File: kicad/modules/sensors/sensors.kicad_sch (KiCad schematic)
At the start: 48 parts, among them J1 Bus_PCI_Express_x1, J2 TYPE-C-31-M-04, J4 Conn_01x02, U2 RP2040, U4 W25Q128JVP, U5 BMP388, U8 BNO055, U9 MCP25625T-E/ML, X1 ABM8-272-T3, Y1 ABS07-32.768KHZ-T, Y2 X322516MLB4SI

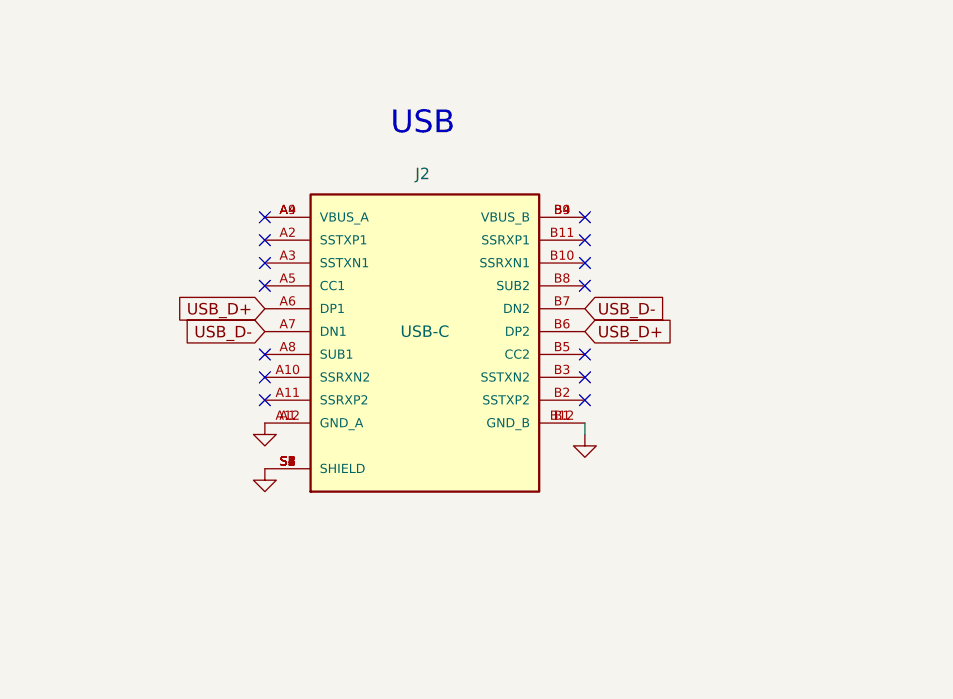
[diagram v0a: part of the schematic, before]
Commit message: change USB-C connector
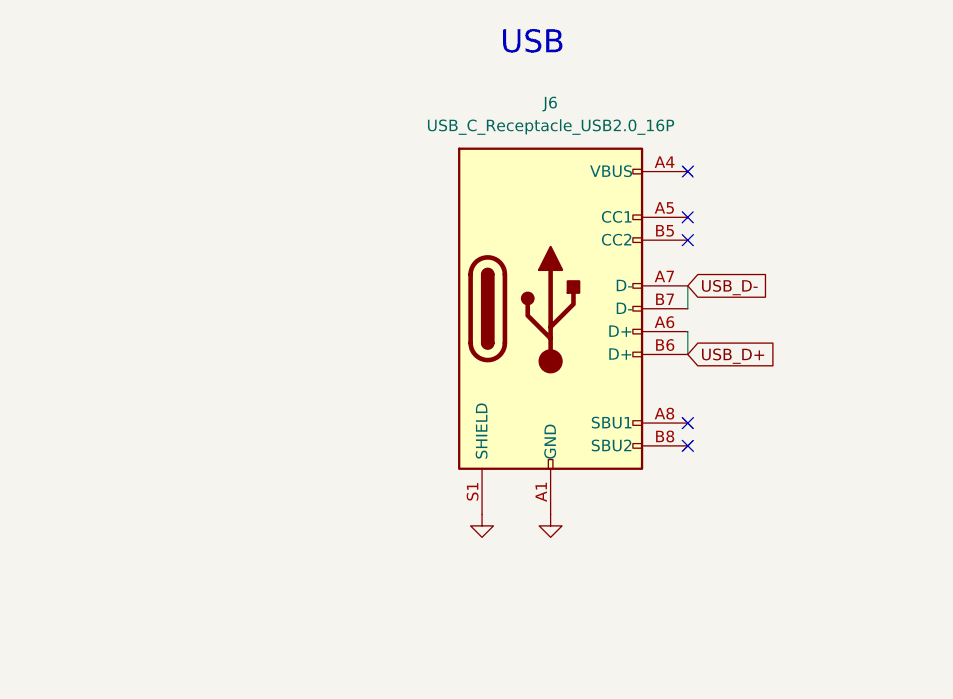
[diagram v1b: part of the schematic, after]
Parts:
- removed J2: TYPE-C-31-M-04, TYPE-C-31-M-04:HRO_TYPE-C-31-M-04, symbol TYPE-C-31-M-04:TYPE-C-31-M-04
- added J6: USB_C_Receptacle_USB2.0_16P, Connector_USB:USB_C_Receptacle_Palconn_UTC16-G, symbol Connector:USB_C_Receptacle_USB2.0_16P
- R203, R204: footprint Resistor_SMD:R_0603_1608Metric -> Resistor_SMD:R_0402_1005Metric; JLC Link https://jlcpcb.com/partdetail/25933-0603WAF270JT5E/C25190 -> https://jlcpcb.com/partdetail/25843-0402WGF270JTCE/C25100; LCSC Part # C25190 -> C25100; basic? extended prefered -> no; price C$0.0013 -> C$0.0007
- S1, S2: price C$0.0242 -> C$0.0242
- U5: price C$2.3423 -> C$2.3423
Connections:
- net GND: now also J6.A1 (GND), J6.A12 (GND), J6.B1 (GND), J6.B12 (GND), J6.S1 (SHIELD)
- net USB_D+: now also J6.A6 (D+), J6.B6 (D+)
- net USB_D-: now also J6.A7 (D-), J6.B7 (D-)
- new net: J6.A4 (VBUS), J6.A9 (VBUS), J6.B4 (VBUS), J6.B9 (VBUS)
- no-connect marks 20 -> 11

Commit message: route under rp2040
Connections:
- net USB_D2-: now reaches R204.2, U2.46 (USB_DM)
- net USB_D2+: now reaches R203.2, U2.47 (USB_DP)
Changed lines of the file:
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@@
+		)
+	)
+	(label "USB_D2+"
+		(at 262.89 151.13 0)
+		(fields_autoplaced yes)
+		(effects
+			(font
+				(size 1.27 1.27)
+			)
+			(justify left bottom)
 		)
 	)
@@
 		(fields_autoplaced yes)
 		(effects
+			(font
+				(size 1.27 1.27)
+			)
+			(justify left bottom)
+		)
+	)
+	(label "USB_D2-"
+		(at 262.89 153.67 0)
+		(fields_autoplaced yes)
+		(effects

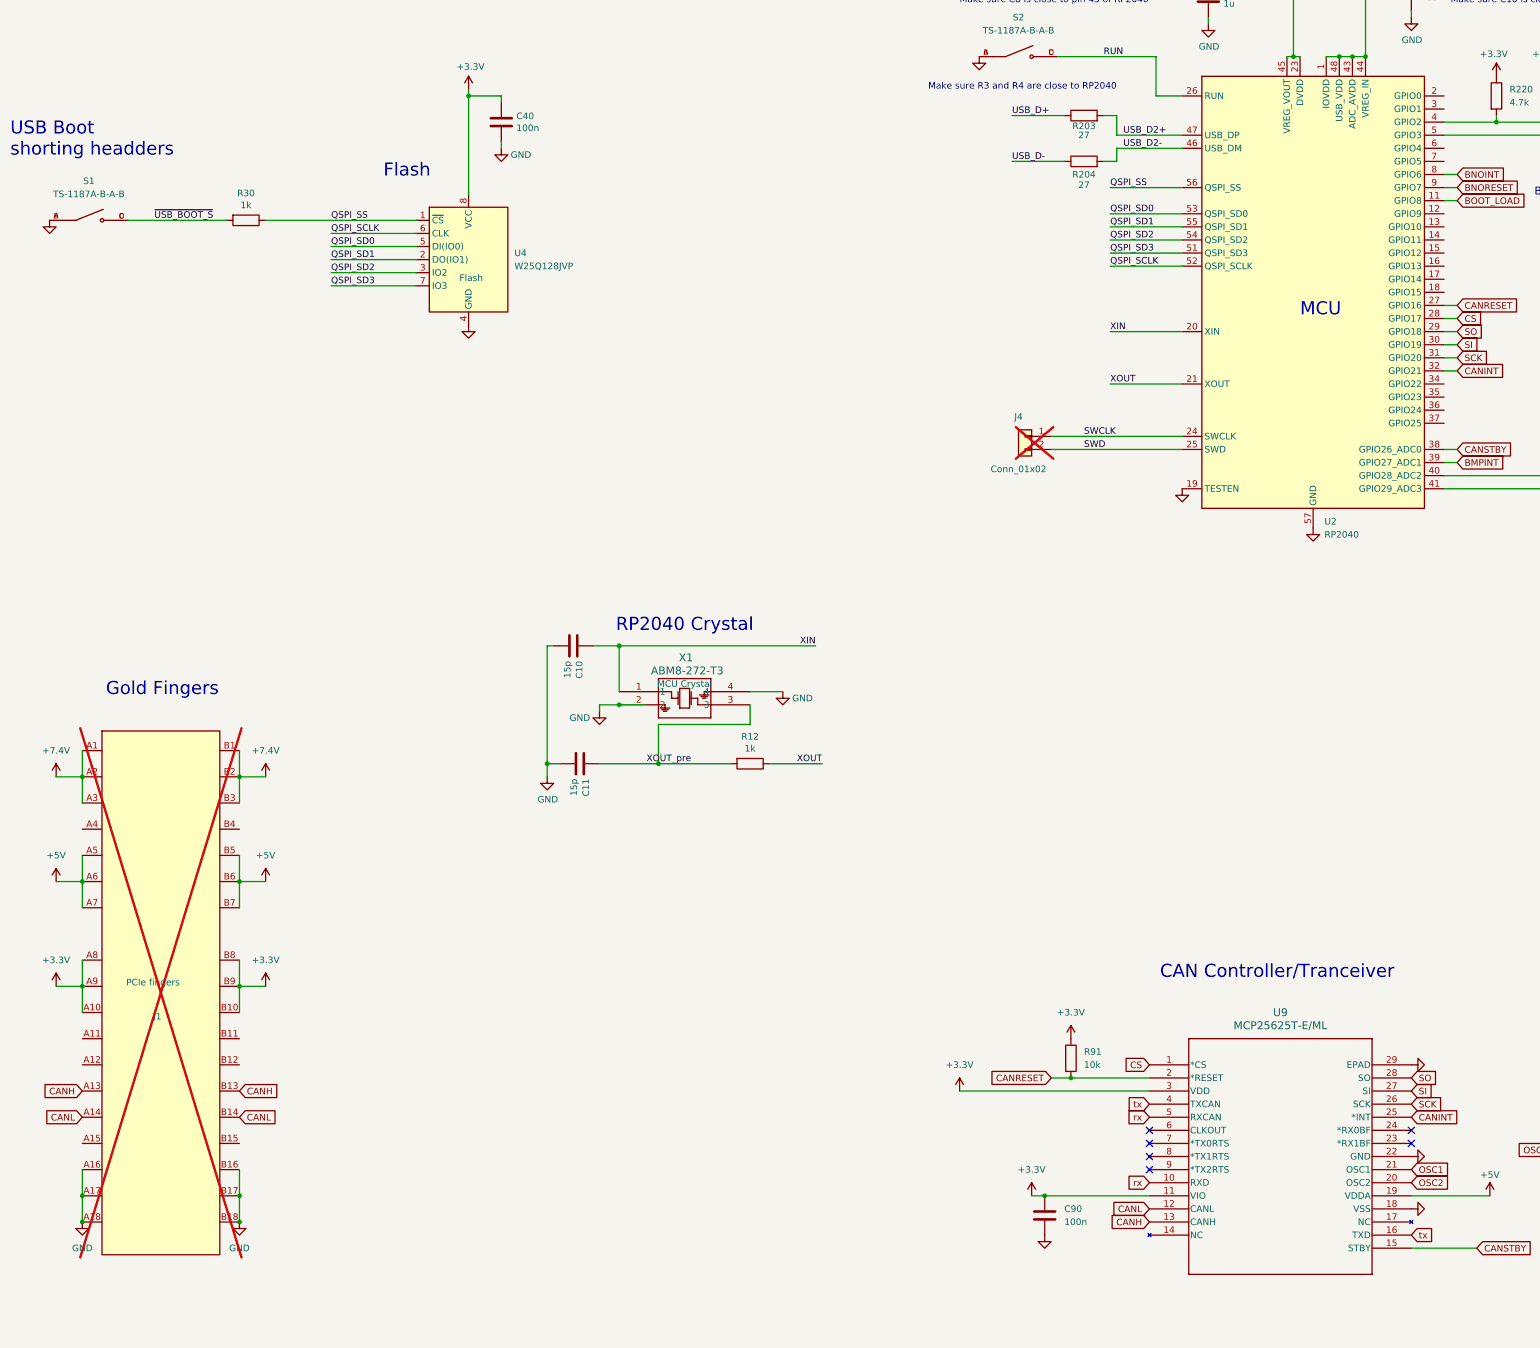
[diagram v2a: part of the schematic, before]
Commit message: complete all routing connections, and planes
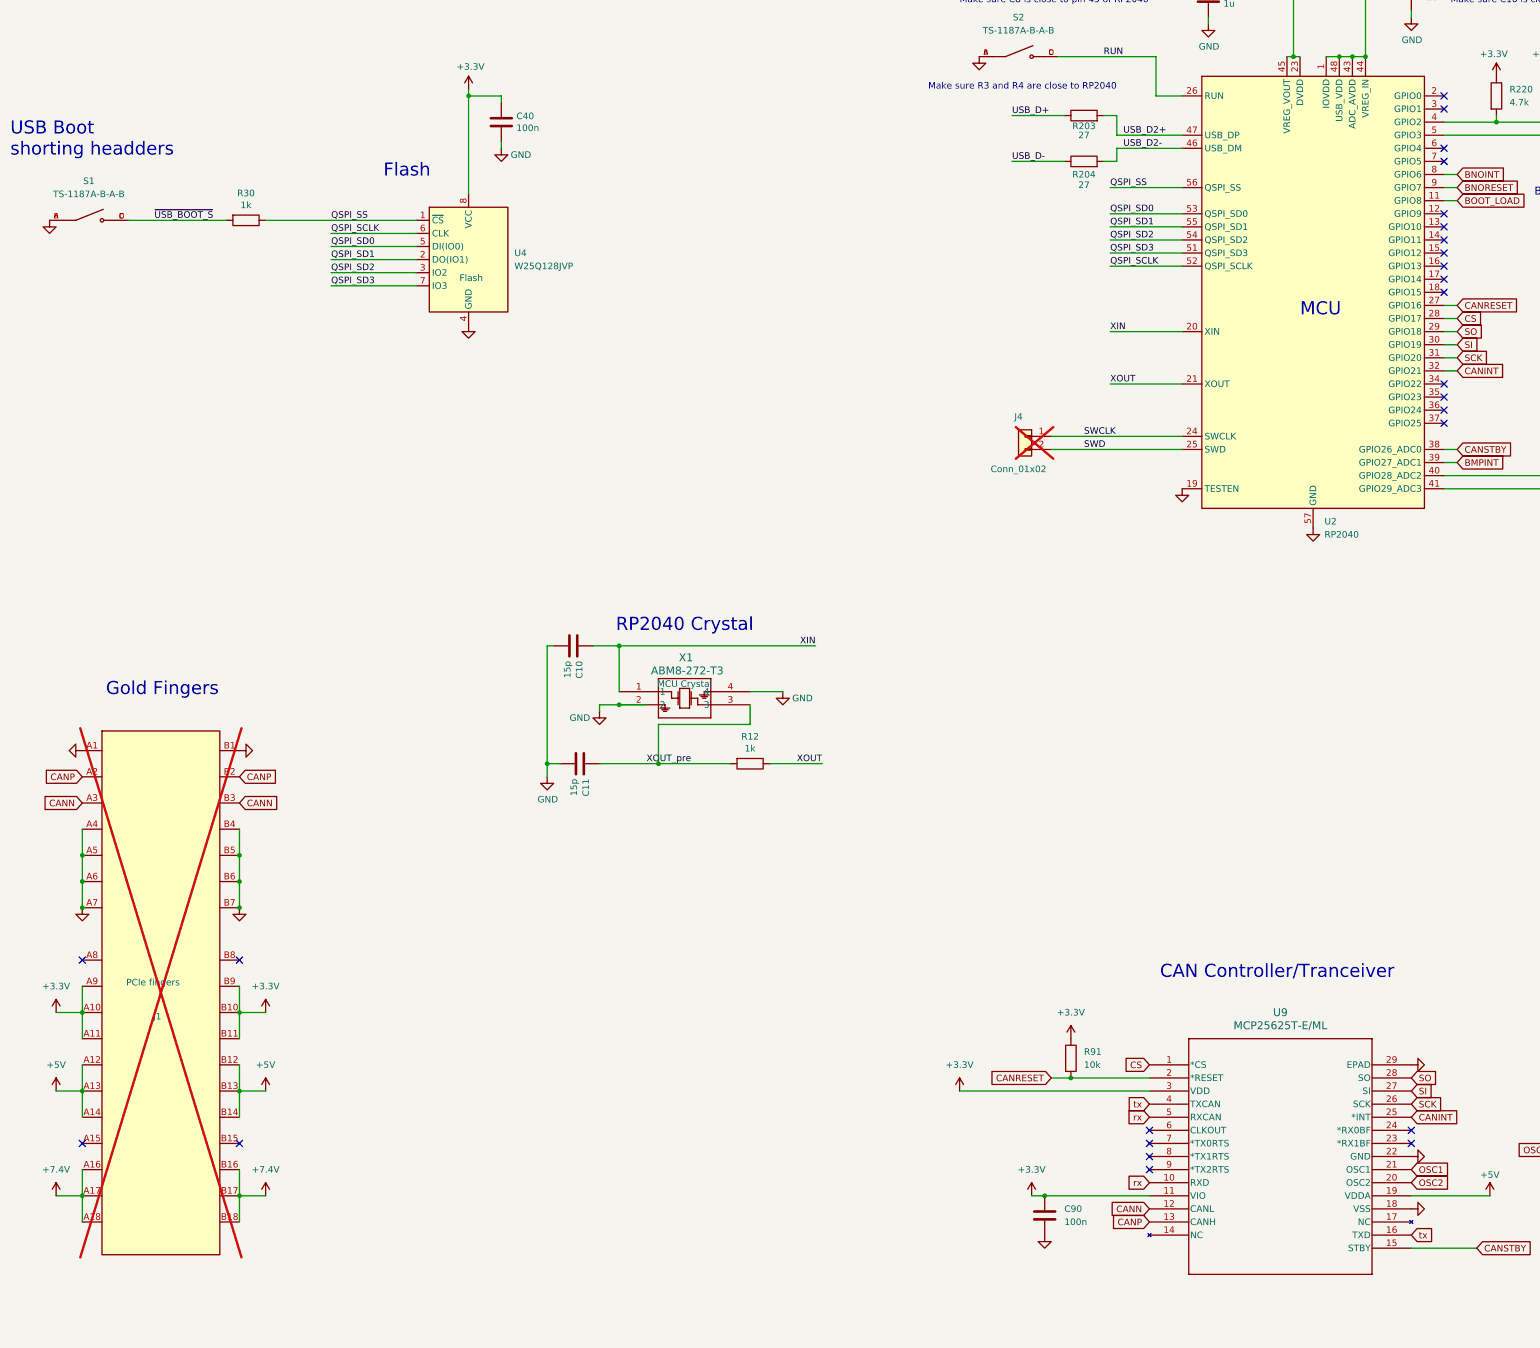
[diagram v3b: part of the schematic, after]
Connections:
- net +3.3V: now also J1.A11 (~{PERST}), J1.B11 (~{WAKE}); no longer J1.A8 (JTAG5), J1.B8 (+3.3V)
- net +5V: now also J1.A12 (GND), J1.A13 (REFCLK+), J1.A14 (REFCLK-), J1.B12 (RSVD), J1.B13 (GND), J1.B14 (PETp0); no longer J1.A5 (JTAG2), J1.A6 (JTAG3), J1.A7 (JTAG4), J1.B5 (SMCLK), J1.B6 (SMDAT), J1.B7 (GND)
- net +7.4V: now also J1.A16 (PERp0), J1.A17 (PERn0), J1.A18 (GND), J1.B16 (GND), J1.B17 (~{PRSNT2}), J1.B18 (GND); no longer J1.A1 (~{PRSNT1}), J1.A2 (+12V), J1.A3 (+12V), J1.B1 (+12V), J1.B2 (+12V), J1.B3 (+12V)
- net GND: now also J1.A1 (~{PRSNT1}), J1.A4 (GND), J1.A5 (JTAG2), J1.A6 (JTAG3), J1.A7 (JTAG4), J1.B1 (+12V), J1.B4 (GND), J1.B5 (SMCLK), J1.B6 (SMDAT), J1.B7 (GND); no longer J1.A16 (PERp0), J1.A17 (PERn0), J1.A18 (GND), J1.B16 (GND), J1.B17 (~{PRSNT2}), J1.B18 (GND)
- removed net CANH: J1.A13 (REFCLK+), J1.B13 (GND), U9.13 (CANH)
- removed net CANL: J1.A14 (REFCLK-), J1.B14 (PETp0), U9.12 (CANL)
- new net CANN: J1.A3 (+12V), J1.B3 (+12V), U9.12 (CANL)
- new net CANP: J1.A2 (+12V), J1.B2 (+12V), U9.13 (CANH)
- no-connect marks 11 -> 30

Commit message: refine routing
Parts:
- added C92, C93: 100n, Capacitor_SMD:C_0402_1005Metric, symbol Device:C
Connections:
- net +3.3V: now also C92.1
- net +5V: now also C93.1
- net GND: now also C92.2, C93.2
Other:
- note added: "Make sure C210 is close to pin 44 of RP2040"
- note removed: "Make sure C10 is close to pin 44 of RP2040"

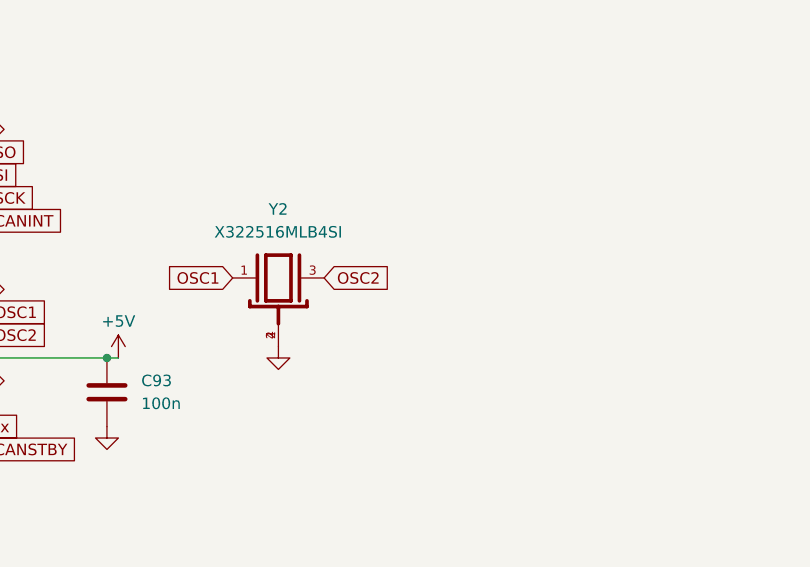
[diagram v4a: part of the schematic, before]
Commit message: finish diff pairs and planes
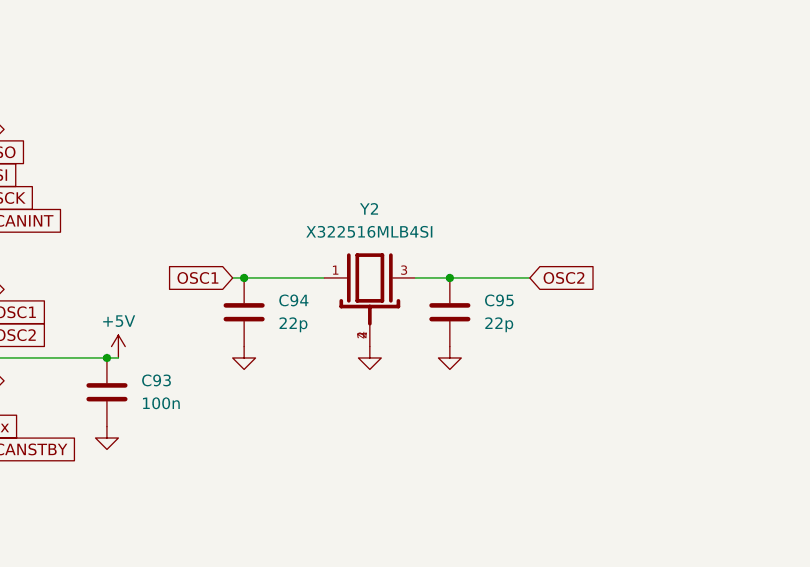
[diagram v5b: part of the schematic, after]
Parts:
- added C94, C95: 22p, Capacitor_SMD:C_0402_1005Metric, symbol Device:C
- C85, C86: price C$0.0013 -> C$0.0077
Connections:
- net GND: now also C94.2, C95.2
- net OSC1: now also C94.1
- net OSC2: now also C95.1
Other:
- moved on the sheet: Y2
